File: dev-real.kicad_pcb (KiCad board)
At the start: 4 copper layers, 105 x 105 mm, 318 parts, among them IC1 ICM-42670-P, IC2 ENS161-BLGT_LGA9_T&R_1k5, J1 VIN_IN, J10 USB-C USB2 DEBUG, J11 ARM_JTAG_10, J12 SOP0_SELECT, J13 SOP1_SELECT, J14 Conn_01x03, J15 Conn_01x03, J16 ARM_JTAG_10, J17 USB-C Receptacle USB2, J18 Conn_01x03_Pin, J19 Cortex SWD/JTAG, J2 TP_EN_PG, J20 USB-C USB2 DEVICE, J21 HR911105A MAGJACK, J22 Conn_02x10_Counter_Clockwise, J23 Conn_02x04_Odd_Even, J3 TP_SW_FB, J4 USB-C Receptacle USB2, J5 Conn_01x03_Pin, J6 ARM_Cortex_Debug_10, J7 SMA_ANT_50OHM, J8 3V3_IN, U1 MMC5633NJL, U10 USBLC6-2P6, U11 FT230XS-R, U12 FT230XS-R, U13 IWRL6432BDBAAMFR, U14 MX25R1635FZUIH0, U15 MX25R1635FZUIH0, U16 AMS1117-1.8, U17 THS8136, U18 MM8108-MF15457, U19 AP2112K-1.8, U2 LPS22HH, U20 PGA113AIDGSR, U21 AD9609BCPZRL7-80, U22 MCP6D11T-E/MS, U23 STM32H7S3Z8T6, U24 LAN8742A-CZ-TR, U25 USBLC6-2SC6, U3 MIC28516T-E/PHA, U4 RP2350B, U5 XCC1352R1F3RGZR, U6 XMSSJJ3G0PA-054, U7 TLV75518PDBV, U8 TLV75518PDBVR, U9 USBLC6-2P6, Y1 12MHz ABM8-272-T3, Y2 48MHz, Y3 40MHz, Y4 40MHz, Y5 24MHz, Y6 32.768kHz, Y7 25MHz

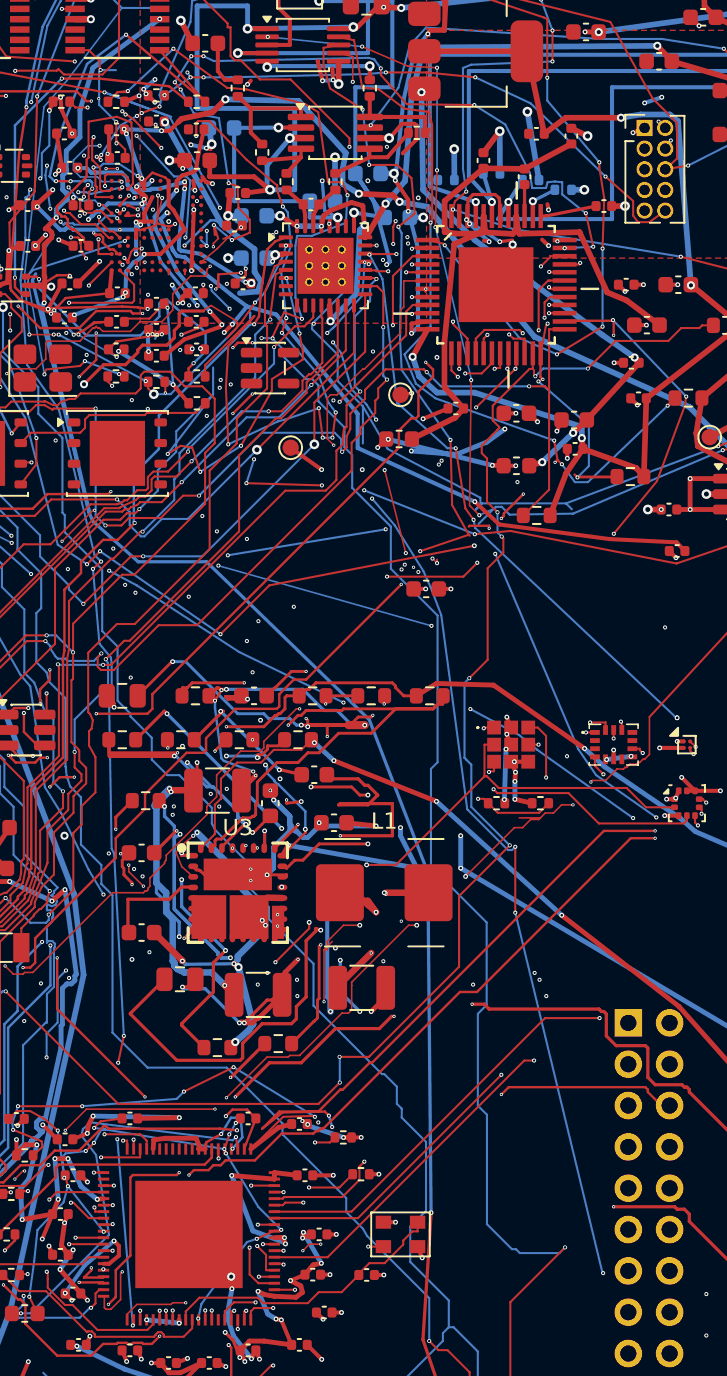
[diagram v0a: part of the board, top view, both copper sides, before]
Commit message: Fix all remaining unconnected items on dev-real.kicad_pcb
Resolved the last 6 connectivity gaps around the U13 radar BGA corner
(GND ball M12, an In2/GND stub near (56.9,16.0), C34 pad 1, U21 pad
26, a split GND plane island on In1, and an NRESET In1<->F gap), each
fixed and verified against real kicad-cli DRC individually. Most
needed via-in-pad connections plus small local shoves of neighboring
nets (FT_RXD, GPIO_4) that were routed directly under the affected
pads, since escape-track congestion in that corner defeats the
default interactive shove router.

Both boards are now fully clean: dev-real.kicad_pcb and
dev-real-production.kicad_pcb are each at 0 DRC violations, 0
unconnected items.

README.md updated to reflect the board is fully routed; the stale
per-item GUI-fix table was replaced with a historical summary.

Co-Authored-By: Claude Sonnet 5 <noreply@anthropic.com>
Claude-Session: https://claude.ai/code/session_0186Z8rzxmfg6xURJrUFb6p5
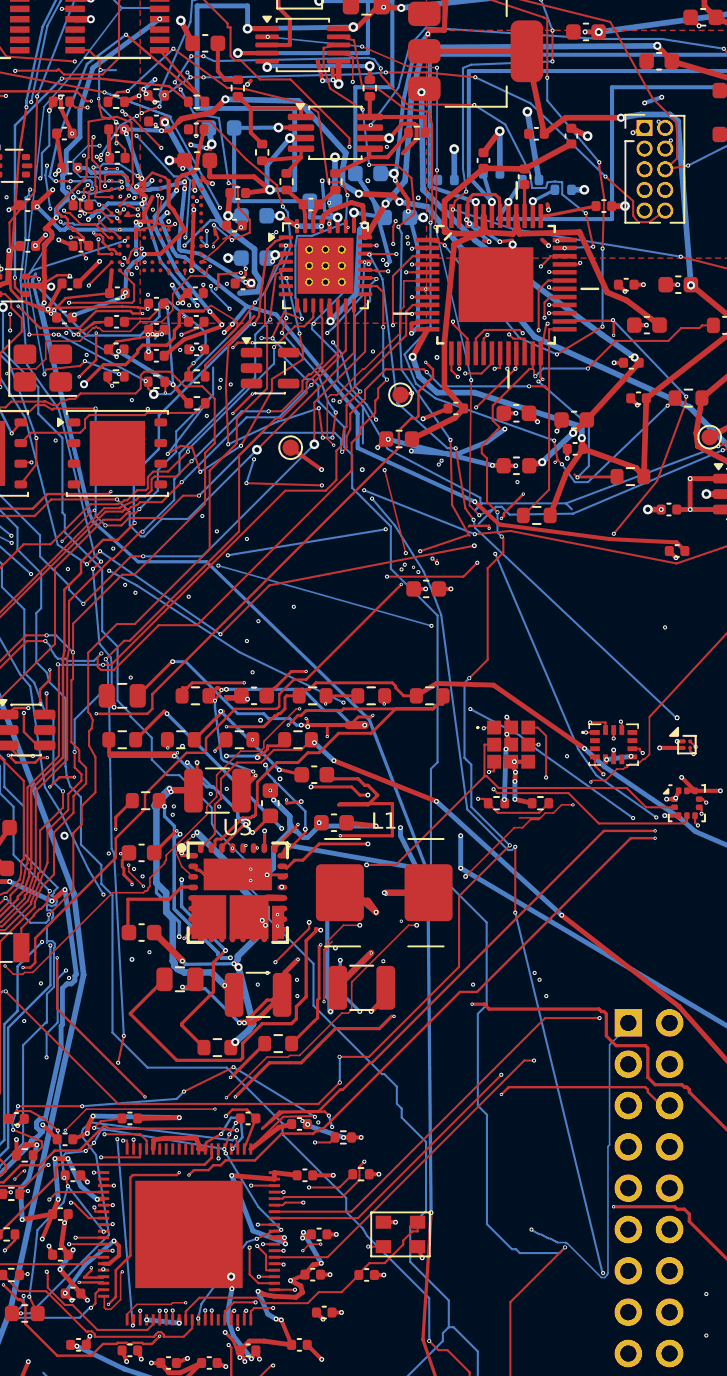
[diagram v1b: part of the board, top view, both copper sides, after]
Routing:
- net GND: track 1639.7 -> 1670.6 mm, vias 355 -> 360
- net /IWRL6432BD/NRESET: track 58.3 -> 60.4 mm
